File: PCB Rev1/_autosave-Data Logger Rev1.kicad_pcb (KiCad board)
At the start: 2 copper layers, 4 parts, among them J1 MICRO_SD, U1 SAM-M10Q, U2 ESP32-PICO-V3-ZERO, U3 AP22653QW6-7

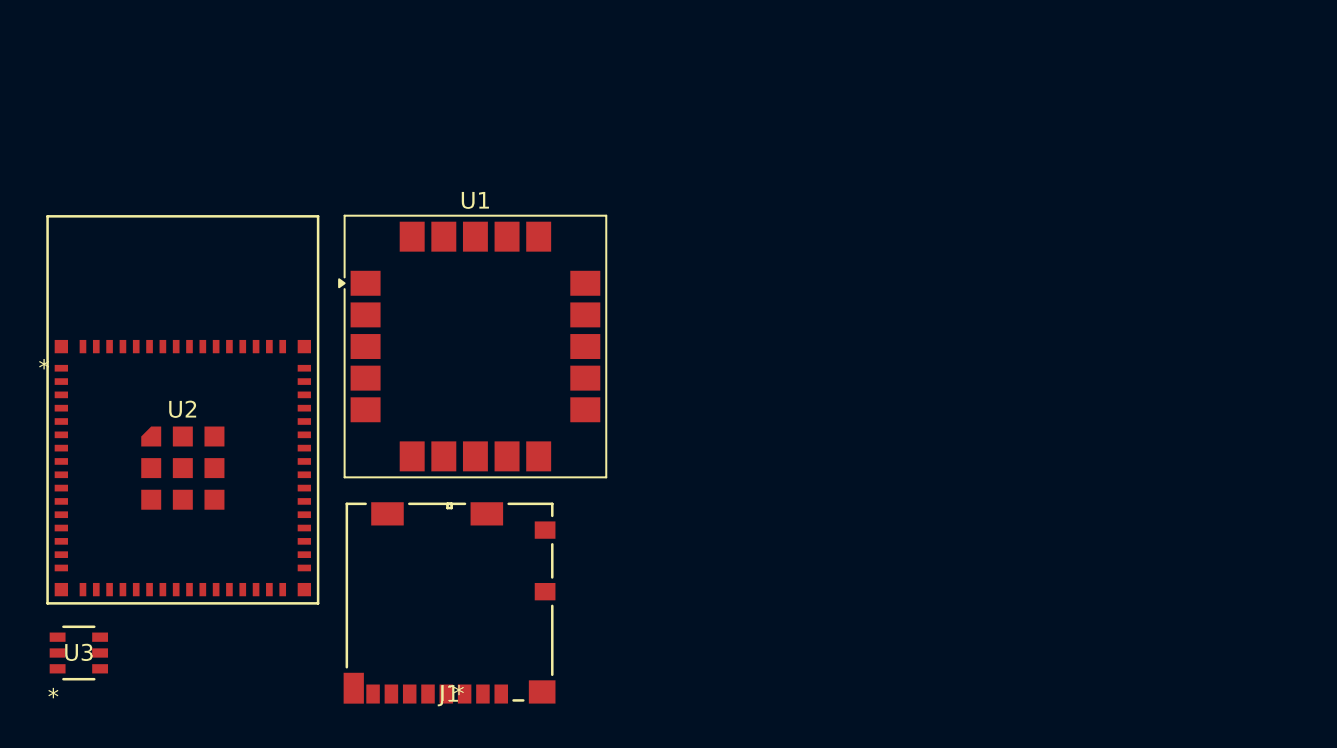
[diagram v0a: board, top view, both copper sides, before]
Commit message: Added power filtering stage 1, DC->DC Buck
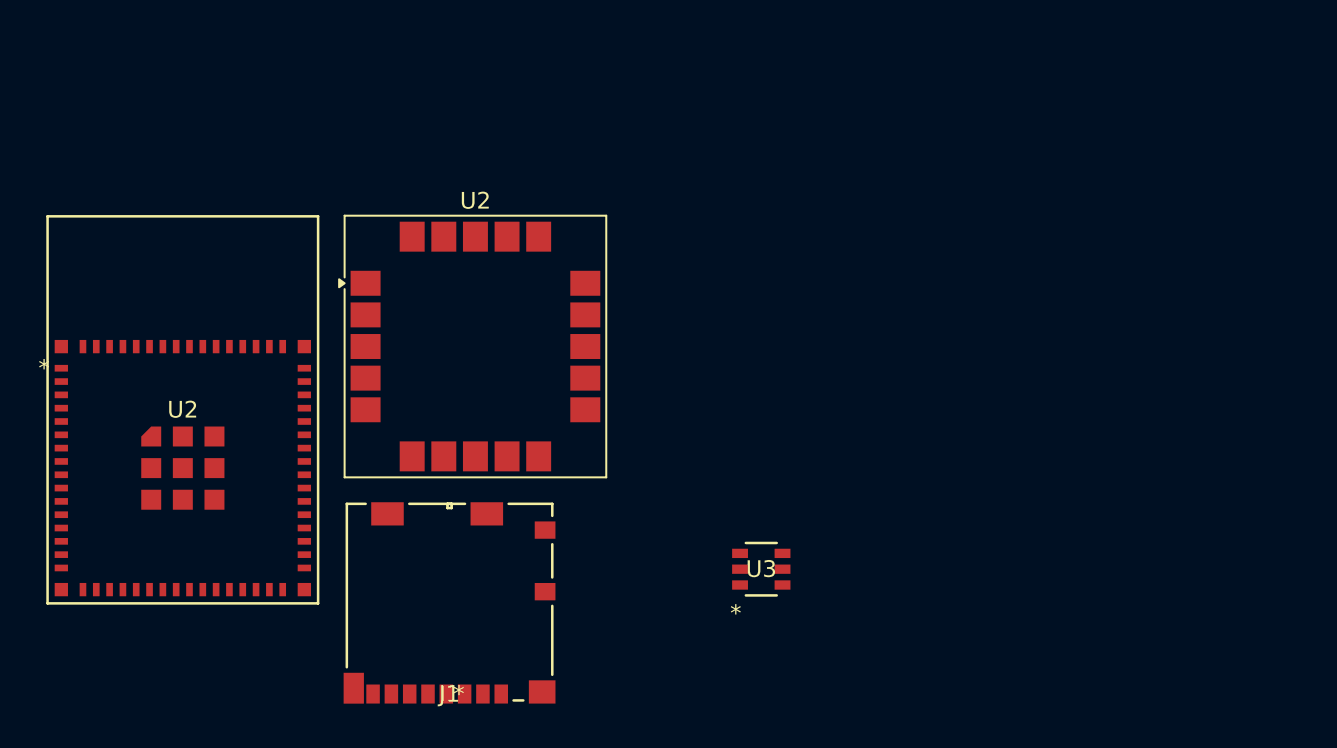
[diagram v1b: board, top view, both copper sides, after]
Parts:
- moved U3 41.3 mm to (155.7, 103.5)
- renumbered U1 to U2
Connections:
- J1 pad 1: unconnected-(J1-DAT2-Pad1) -> /GPIO42
- J1 pad 10: unconnected-(J1-SW_DETECT-Pad10) -> GND
- J1 pad 2: unconnected-(J1-CD/DAT3-Pad2) -> /GPIO35
- J1 pad 3: unconnected-(J1-CMD-Pad3) -> /GPIO37
- J1 pad 4: unconnected-(J1-VDD-Pad4) -> /power_switch/out
- J1 pad 5: unconnected-(J1-CLK-Pad5) -> /GPIO36
- J1 pad 6: unconnected-(J1-VSS-Pad6) -> GND
- J1 pad 7: unconnected-(J1-DAT0-Pad7) -> /GPIO38
- J1 pad 8: unconnected-(J1-DAT1-Pad8) -> /GPIO39
- J1 pad 9: unconnected-(J1-SW_DETECT-Pad9) -> /GPIO1
- U2 pad 1: Net-(U1-GND-Pad1) -> GND
- U2 pad 10: Net-(U1-GND-Pad1) -> GND
- U2 pad 11: Net-(U1-GND-Pad1) -> GND
- U2 pad 12: unconnected-(U1-SCL-Pad12) -> /GPIO9
- U2 pad 15: Net-(U1-GND-Pad1) -> GND
- U2 pad 16: Net-(U1-GND-Pad1) -> GND
- U2 pad 17: unconnected-(U1-VCC-Pad17) -> Net-(U2-VCC)
- U2 pad 2: unconnected-(U1-VCC_IO-Pad2) -> Net-(U2-VCC)
- U2 pad 20: Net-(U1-GND-Pad1) -> GND
- U2 pad 3: unconnected-(U1-V_BCKP-Pad3) -> GND
- U2 pad 4: Net-(U1-GND-Pad1) -> GND
- U2 pad 5: Net-(U1-GND-Pad1) -> GND
- U2 pad 6: Net-(U1-GND-Pad1) -> GND
- U2 pad 9: unconnected-(U1-SDA-Pad9) -> /GPIO8
- U3 pad 1: unconnected-(U3-in-Pad1) -> +3.3V
- U3 pad 2: unconnected-(U3-gnd-Pad2) -> GND
- U3 pad 3: unconnected-(U3-en-Pad3) -> /power_switch/en
- U3 pad 4: unconnected-(U3-*fault-Pad4) -> Net-(U3-*fault)
- U3 pad 5: unconnected-(U3-ilim-Pad5) -> Net-(U3-ilim)
- U3 pad 6: unconnected-(U3-out-Pad6) -> /power_switch/out

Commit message: Progress marches on.
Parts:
- removed U2: SAM-M10Q, RF_GPS:ublox_SAM-M8Q
- removed U2: ESP32-PICO-V3-ZERO, footprints:ESP32-PICO-V3-ZERO_EXP
- added D1: TVS, Diode_SMD:D_SMA, F.Cu at (144.5, 100.0)
- added D2: TVS, Diode_SMD:D_SMA, F.Cu at (144.5, 104.5)
- added D3: TVS, Diode_SMD:D_SMA, F.Cu at (144.5, 109.1)
- added J2: USB_B_Micro, Connector_USB:USB_Micro-B_Amphenol_10118193-0001LF_Horizontal, F.Cu at (131.5, 99.2)
- added J3: Conn_01x02_Socket, Connector_PinSocket_2.54mm:PinSocket_1x02_P2.54mm_Vertical, F.Cu at (131.5, 76.5)
- added U1: ESP32-S3-MINI-1U-N8, footprints:ESP32-S3-MINI-1U_EXP, F.Cu at (152.2, 79.2)
- added U4: LMR43620MSC3RPERQ1, footprints:RPE0009A-MFG, F.Cu at (184.6, 99.7)
- added U5: TPS2116DRL, Package_TO_SOT_SMD:SOT-583-8, F.Cu at (179.1, 87.4)
- added U7: LT3042EDD_PBF, footprints:VREG_LT3042EDD_PBF, F.Cu at (146.5, 92.0)
- added U8: SAM-M10Q, RF_GPS:ublox_SAM-M8Q, F.Cu at (171.6, 99.8)
- moved J1 42.6 mm to (170.0, 78.6)
- moved U3 30.6 mm to (184.7, 93.5)
